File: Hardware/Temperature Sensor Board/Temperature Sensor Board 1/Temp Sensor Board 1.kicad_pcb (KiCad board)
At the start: 2 copper layers, 41.3 x 19.9 mm, 3 parts, among them J1 6P6C

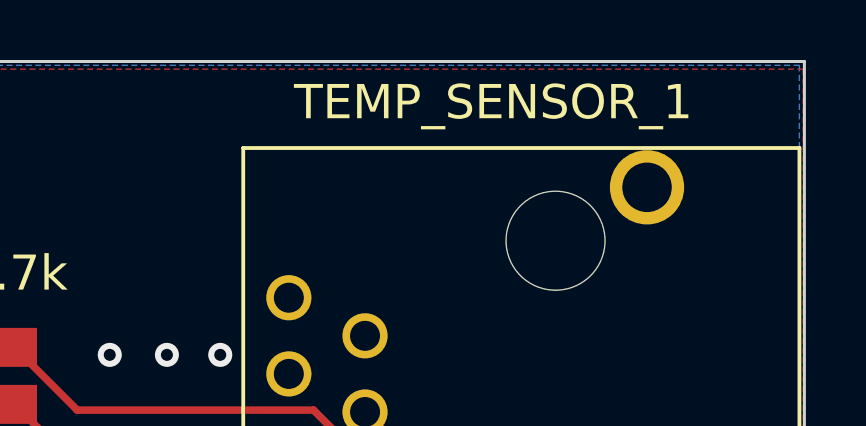
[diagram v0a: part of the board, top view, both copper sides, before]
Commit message: complete gerber for temp sensors
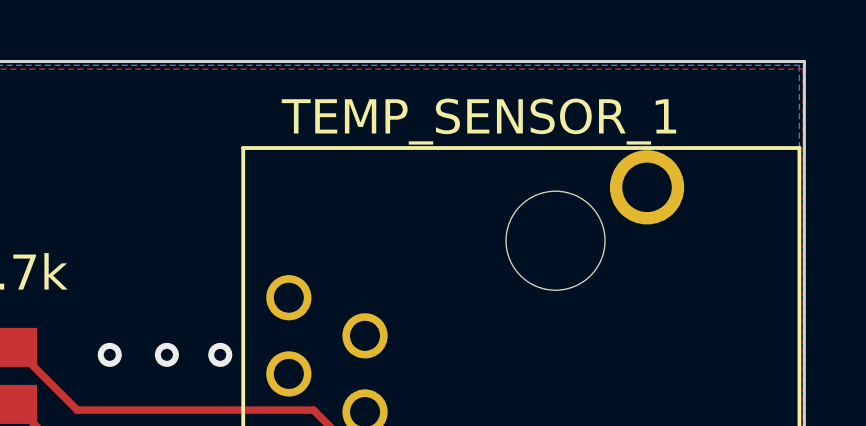
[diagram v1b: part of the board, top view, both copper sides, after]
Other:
- board text added: "DQ"
- board text added: "VDD"
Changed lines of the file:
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@@
       (plot_on_all_layers_selection 0x0000000_00000000)
       (disableapertmacros false)
-      (usegerberextensions false)
-      (usegerberattributes true)
-      (usegerberadvancedattributes true)
-      (creategerberjobfile true)
+      (usegerberextensions true)
+      (usegerberattributes false)
+      (usegerberadvancedattributes false)
+      (creategerberjobfile false)
       (dashed_line_dash_ratio 12.000000)
       (dashed_line_gap_ratio 3.000000)
@@
       (psa4output false)
       (plotreference true)
-      (plotvalue true)
+      (plotvalue false)
       (plotinvisibletext false)
       (sketchpadsonfab false)
-      (subtractmaskfromsilk false)
+      (subtractmaskfromsilk true)
       (outputformat 1)
       (mirror false)
       (drillshape 0)
       (scaleselection 1)
-      (outputdirectory "../../Documents/GitHub/AutomatedLoadBank/Hardware/Temperature Sensor Board/Gerber File (4)/")
+      (outputdirectory "temp_sens1_gerber/")
     )
   )
@@
   (gr_rect (start 117.221 72.517) (end 158.536646 92.369646)
     (stroke (width 0.1) (type default)) (fill none) (layer "Edge.Cuts"))
-  (gr_text "TEMP_SENSOR_1" (at 154.813 74.549) (layer "F.SilkS")
+  (gr_text "VDD" (at 144.8562 84.709) (layer "B.SilkS")
+    (effects (font (size 1 1) (thickness 0.1)) (justify right bottom mirror))
+  )
+  (gr_text "DQ\n" (at 146.9644 87.1474) (layer "B.SilkS")
+    (effects (font (size 1 1) (thickness 0.1)) (justify left bottom mirror))
+  )
+  (gr_text "TEMP_SENSOR_1" (at 154.4066 75.057) (layer "F.SilkS")
     (effects (font (size 1.143 1.143) (thickness 0.127)) (justify right bottom))
   )
